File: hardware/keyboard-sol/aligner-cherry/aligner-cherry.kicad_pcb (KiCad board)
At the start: 2 copper layers, 386.1 x 117.7 mm, 94 parts, among them SW10 TAB: 1.25x, SW11 I, SW12 2, SW13 Zero, SW14 Q, SW15 O, SW16 3, SW17 Dash, SW18 W, SW19 P, SW20 4, SW21 Caret, SW22 E, SW23 AT, SW24 5, SW25 LT Bracket, SW26 R, SW27 Return: 1.5x, SW28 6, SW29 Backslash, SW30 T, SW31 Line Feed, SW32 7, SW33 RT Bracket, SW34 Y, SW35 Load, SW36 LT Ctrl, SW37 J, SW38 Upper Case: 1.5x, SW39 M, SW4 ESC: 1.75x, SW40 Shift Lock: 1.5x, SW41 K, SW42 LT Shift: 1.5x, SW43 Comma, SW44 A, SW45 L, SW46 Z, SW47 Period, SW48 S, SW49 Semicolon, SW5 8, SW50 X, SW51 Slash, SW52 D, SW53 Colon, SW54 C, SW55 RT Shift: 2x, SW56 F, SW57 DEL, SW58 V, SW59 Mode Select: 1.75x, SW6 BREAK, SW60 G, SW61 Repeat: 1.25x, SW62 B, SW63 H, SW64 RT Ctrl, SW65 N, SW66 Local, SW67 NP Dash, SW68 NP 4, SW69 NP Zero, SW7 U, SW70 Up Arrow, SW71 NP 7, SW72 NP 1, SW73 NP period, SW74 LT Arrow, SW75 NP asterisk, SW76 NP 5, SW77 NP plus, SW78 Spacebar, SW79 NP 8, SW8 1, SW80 NP 2, SW81 RT Arrow, SW82 NP divide, SW83 NP 6, SW84 Down Arrow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

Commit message: Moved mounting slots from keyboard PCB to aligners
- This allows the PCB to sink below the mounting brackets.  The aligner height can
be adjusted relative to the mounting brackets using spacers.

- changed futaba aligners to use cherry stabilizers.

- bumped rev number
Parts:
- SW55: footprint unikbd:Key_MX_Aligner -> unikbd:MX_2u_aligner
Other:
- board size 386.1 x 117.7 mm -> 428.6 x 117.7 mm
- board text added: "SOL-20 Cherry MX aligner Rev 1.1"
- board text removed: "SOL-20 Cherry MX aligner Rev 1.0"

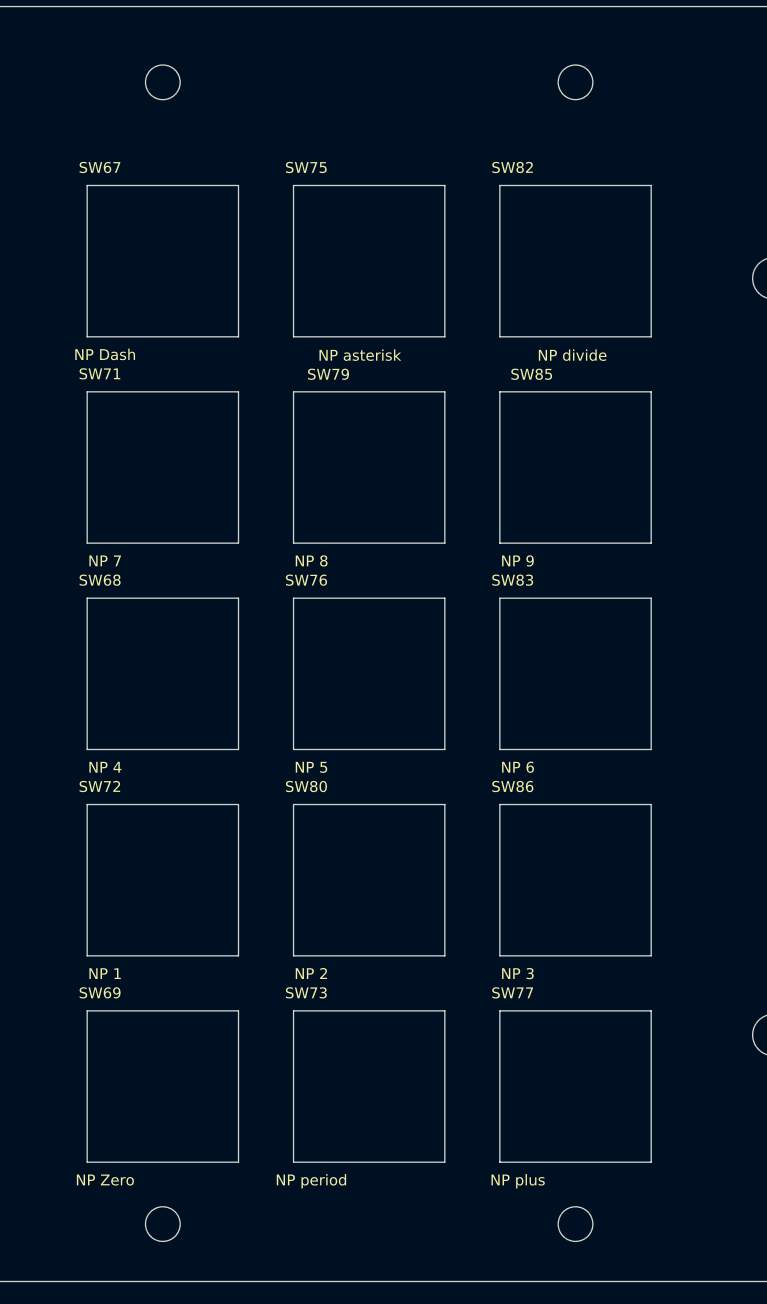
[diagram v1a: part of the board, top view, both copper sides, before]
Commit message: On aligners, moved numpad 0.1825" to the right.
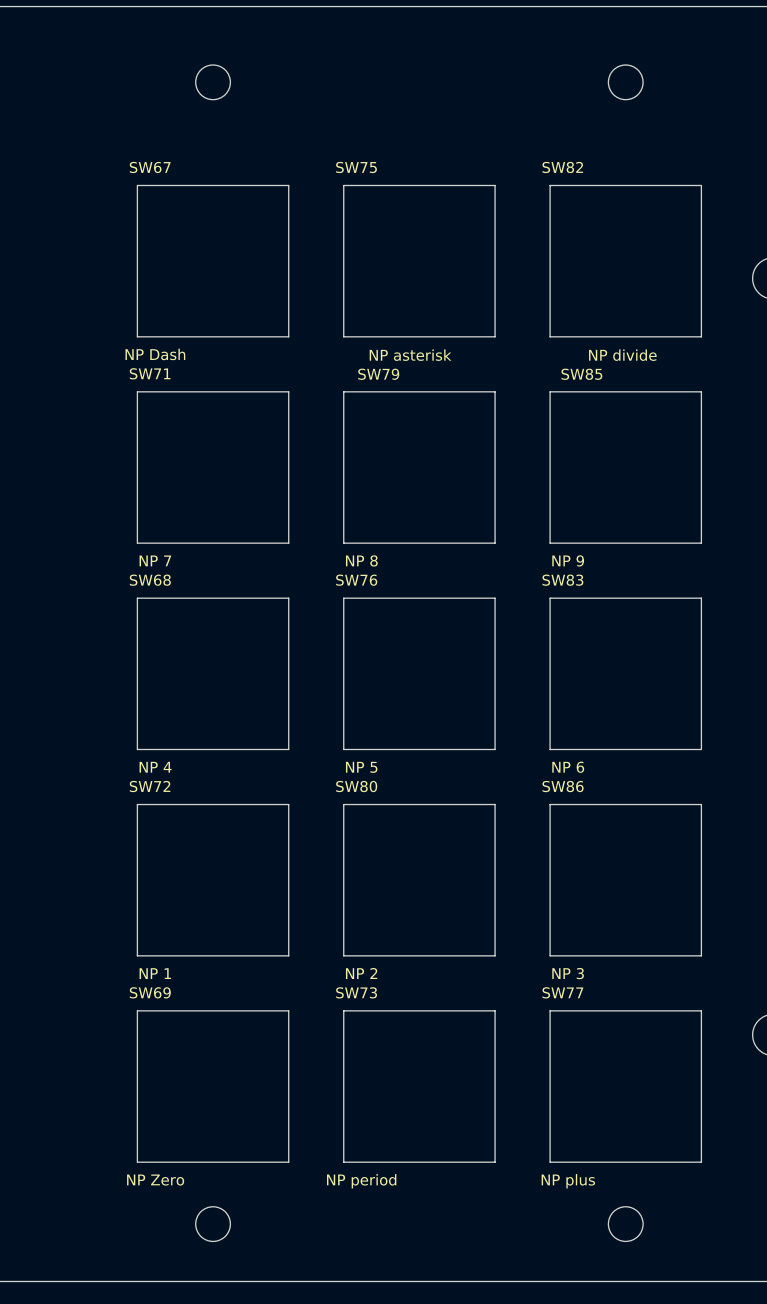
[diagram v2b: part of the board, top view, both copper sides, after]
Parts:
- removed the REF** at (432.4, 219.5)
- removed the REF** at (470.5, 219.5)
- removed the REF** at (470.5, 114.1)
- removed the REF** at (432.4, 114.1)
- added REF**: MountingHole_3.2mm_M3, MountingHole:MountingHole_3.2mm_M3, F.Cu at (437.1, 219.5)
- added REF**: MountingHole_3.2mm_M3, MountingHole:MountingHole_3.2mm_M3, F.Cu at (475.2, 219.5)
- added REF**: MountingHole_3.2mm_M3, MountingHole:MountingHole_3.2mm_M3, F.Cu at (475.2, 114.1)
- added REF**: MountingHole_3.2mm_M3, MountingHole:MountingHole_3.2mm_M3, F.Cu at (437.1, 114.1)
- moved SW73 4.64 mm to (456.1, 206.8)
- moved SW75 4.64 mm to (456.1, 130.6)
- moved SW76 4.64 mm to (456.1, 168.7)
- moved SW79 4.64 mm to (456.1, 149.6)
- moved SW80 4.64 mm to (456.1, 187.7)
- moved SW67 4.64 mm to (437.1, 130.6)
- moved SW68 4.64 mm to (437.1, 168.7)
- moved SW69 4.64 mm to (437.1, 206.8)
- moved SW71 4.64 mm to (437.1, 149.6)
- moved SW72 4.64 mm to (437.1, 187.7)
- moved SW77 4.64 mm to (475.2, 206.8)
- moved SW82 4.64 mm to (475.2, 130.6)
- moved SW83 4.64 mm to (475.2, 168.7)
- moved SW85 4.64 mm to (475.2, 149.6)
- moved SW86 4.64 mm to (475.2, 187.7)
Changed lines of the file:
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@@
   )
   (module unikbd:Key_MX_Aligner locked (layer F.Cu)
-    (at 451.47738 168.69156)
+    (at 456.11288 168.69156)
     (fp_text reference SW76 (at -5.7912 -8.6106) (layer F.SilkS)
       (effects (font (size 1 1) (thickness 0.15)))
@@
   )
   (module unikbd:Key_MX_Aligner locked (layer F.Cu)
-    (at 432.42738 168.69156)
+    (at 437.06288 168.69156)
     (fp_text reference SW68 (at -5.7912 -8.6106) (layer F.SilkS)
       (effects (font (size 1 1) (thickness 0.15)))
@@
   )
   (module unikbd:Key_MX_Aligner locked (layer F.Cu)
-    (at 470.52738 168.69156)
+    (at 475.16288 168.69156)
     (fp_text reference SW83 (at -5.7912 -8.6106) (layer F.SilkS)
       (effects (font (size 1 1) (thickness 0.15)))
@@
   )
   (module unikbd:Key_MX_Aligner locked (layer F.Cu)
-    (at 470.52738 149.64156)
+    (at 475.16288 149.64156)
     (fp_text reference SW85 (at -4.03098 -8.56996) (layer F.SilkS)
       (effects (font (size 1 1) (thickness 0.15)))
@@
   )
   (module unikbd:Key_MX_Aligner locked (layer F.Cu)
-    (at 470.52738 187.74156)
+    (at 475.16288 187.74156)
     (fp_text reference SW86 (at -5.7912 -8.6106) (layer F.SilkS)
       (effects (font (size 1 1) (thickness 0.15)))
@@
   )
   (module unikbd:Key_MX_Aligner locked (layer F.Cu)
-    (at 470.52738 130.59156)
+    (at 475.16288 130.59156)
     (fp_text reference SW82 (at -5.7912 -8.6106) (layer F.SilkS)
       (effects (font (size 1 1) (thickness 0.15)))
@@
   )
   (module unikbd:Key_MX_Aligner locked (layer F.Cu)
-    (at 451.47738 187.74156)
+    (at 456.11288 187.74156)
     (fp_text reference SW80 (at -5.7912 -8.6106) (layer F.SilkS)
       (effects (font (size 1 1) (thickness 0.15)))
@@
   )
   (module unikbd:Key_MX_Aligner locked (layer F.Cu)
-    (at 451.47738 149.64156)
+    (at 456.11288 149.64156)
     (fp_text reference SW79 (at -3.75158 -8.56996) (layer F.SilkS)
       (effects (font (size 1 1) (thickness 0.15)))
@@
   )
   (module unikbd:Key_MX_Aligner locked (layer F.Cu)
-    (at 470.52738 206.79156)
+    (at 475.16288 206.79156)
     (fp_text reference SW77 (at -5.7912 -8.6106) (layer F.SilkS)
       (effects (font (size 1 1) (thickness 0.15)))
@@
   )
   (module unikbd:Key_MX_Aligner locked (layer F.Cu)
-    (at 451.47738 130.59156)
+    (at 456.11288 130.59156)
     (fp_text reference SW75 (at -5.7912 -8.6106) (layer F.SilkS)
       (effects (font (size 1 1) (thickness 0.15)))
@@
   )
   (module unikbd:Key_MX_Aligner locked (layer F.Cu)
-    (at 451.47738 206.79156)
+    (at 456.11288 206.79156)
     (fp_text reference SW73 (at -5.7912 -8.6106) (layer F.SilkS)
       (effects (font (size 1 1) (thickness 0.15)))
@@
   )
   (module unikbd:Key_MX_Aligner locked (layer F.Cu)
-    (at 432.42738 187.74156)
+    (at 437.06288 187.74156)
     (fp_text reference SW72 (at -5.7912 -8.6106) (layer F.SilkS)
       (effects (font (size 1 1) (thickness 0.15)))
@@
   )
   (module unikbd:Key_MX_Aligner locked (layer F.Cu)
-    (at 432.42738 149.64156)
+    (at 437.06288 149.64156)
     (fp_text reference SW71 (at -5.7912 -8.6106) (layer F.SilkS)
       (effects (font (size 1 1) (thickness 0.15)))
@@
   )
   (module unikbd:Key_MX_Aligner locked (layer F.Cu)
-    (at 432.42738 206.79156)
+    (at 437.06288 206.79156)
     (fp_text reference SW69 (at -5.7912 -8.6106) (layer F.SilkS)
       (effects (font (size 1 1) (thickness 0.15)))
@@
   )
   (module unikbd:Key_MX_Aligner locked (layer F.Cu)
-    (at 432.42738 130.59156)
+    (at 437.06288 130.59156)
     (fp_text reference SW67 (at -5.7912 -8.6106) (layer F.SilkS)
       (effects (font (size 1 1) (thickness 0.15)))
@@
   )
   (module MountingHole:MountingHole_3.2mm_M3 locked (layer F.Cu)
-    (at 432.42738 219.49156)
+    (at 437.06288 219.49156)
     (descr "Mounting Hole 3.2mm, no annular, M3")
     (tags "mounting hole 3.2mm no annular m3")
@@
   )
   (module MountingHole:MountingHole_3.2mm_M3 locked (layer F.Cu)
-    (at 470.52738 219.49156)
+    (at 475.16288 219.49156)
     (descr "Mounting Hole 3.2mm, no annular, M3")
     (tags "mounting hole 3.2mm no annular m3")
@@
   )
   (module MountingHole:MountingHole_3.2mm_M3 locked (layer F.Cu)
-    (at 470.52738 114.08156)
+    (at 475.16288 114.08156)
     (descr "Mounting Hole 3.2mm, no annular, M3")
     (tags "mounting hole 3.2mm no annular m3")
@@
   )
   (module MountingHole:MountingHole_3.2mm_M3 locked (layer F.Cu)
-    (at 432.42738 114.08156)
+    (at 437.06288 114.08156)
     (descr "Mounting Hole 3.2mm, no annular, M3")
     (tags "mounting hole 3.2mm no annular m3")

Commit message: Adjsut mounting slots and alignment of mounting holes.
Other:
- outline, holes or cut-outs redrawn
- board text added: "SOL-20 Cherry MX aligner Rev 1.4"
- board text removed: "SOL-20 Cherry MX aligner Rev 1.1"
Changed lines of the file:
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@@
   (gr_circle (center 102.16388 187.74156) (end 105.38968 187.74156) (layer Edge.Cuts) (width 0.12))
   (gr_circle (center 121.21388 168.69156) (end 124.43968 168.69156) (layer Edge.Cuts) (width 0.12))
-  (gr_text "SOL-20 Cherry MX aligner  Rev 1.1\n" (at 140.9954 112.7506) (layer F.SilkS)
+  (gr_text "SOL-20 Cherry MX aligner  Rev 1.4\n" (at 140.9954 112.7506) (layer F.SilkS)
     (effects (font (size 2.032 2.032) (thickness 0.2032)) (justify left))
   )
@@
     (effects (font (size 2.032 2.032) (thickness 0.3048)) (justify left))
   )
-  (gr_line (start 505.45238 107.0864) (end 505.45238 130.27914) (layer Edge.Cuts) (width 0.1016))
-  (gr_line (start 505.45238 200.12914) (end 505.45238 134.08914) (layer Edge.Cuts) (width 0.1016))
-  (gr_line (start 505.45238 224.79) (end 505.45238 203.93914) (layer Edge.Cuts) (width 0.1016))
-  (gr_line (start 488.78109 203.93914) (end 505.44984 203.93914) (layer Edge.Cuts) (width 0.1016))
-  (gr_line (start 488.78109 134.08914) (end 505.44984 134.08914) (layer Edge.Cuts) (width 0.1016))
-  (gr_line (start 488.78109 130.27914) (end 505.44984 130.27914) (layer Edge.Cuts) (width 0.1016))
-  (gr_arc (start 488.78109 132.18414) (end 488.78109 130.27914) (angle -180) (layer Edge.Cuts) (width 0.1016))
-  (gr_line (start 488.78109 200.12914) (end 505.44984 200.12914) (layer Edge.Cuts) (width 0.1016))
-  (gr_arc (start 488.78109 202.03414) (end 488.78109 200.12914) (angle -180) (layer Edge.Cuts) (width 0.1016))
-  (gr_line (start 76.82738 134.08914) (end 76.82738 200.12914) (layer Edge.Cuts) (width 0.1016))
-  (gr_line (start 76.82738 107.0864) (end 76.82738 130.27914) (layer Edge.Cuts) (width 0.1016))
-  (gr_line (start 93.49613 130.27914) (end 76.82738 130.27914) (layer Edge.Cuts) (width 0.1016))
-  (gr_line (start 93.49613 134.08914) (end 76.82738 134.08914) (layer Edge.Cuts) (width 0.1016))
-  (gr_arc (start 93.49613 132.18414) (end 93.49613 130.27914) (angle 180) (layer Edge.Cuts) (width 0.1016))
-  (gr_line (start 93.49613 203.93914) (end 76.82738 203.93914) (layer Edge.Cuts) (width 0.1016))
-  (gr_line (start 93.49613 200.12914) (end 76.82738 200.12914) (layer Edge.Cuts) (width 0.1016))
-  (gr_line (start 76.82738 224.79) (end 76.82738 203.93914) (layer Edge.Cuts) (width 0.1016))
-  (gr_arc (start 93.49613 202.03414) (end 93.49613 200.12914) (angle 180) (layer Edge.Cuts) (width 0.1016))
+  (gr_line (start 505.45238 107.0864) (end 505.45238 132.81914) (layer Edge.Cuts) (width 0.1016))
+  (gr_line (start 505.45238 202.66914) (end 505.45238 136.62914) (layer Edge.Cuts) (width 0.1016))
+  (gr_line (start 505.45238 224.79) (end 505.45238 206.47914) (layer Edge.Cuts) (width 0.1016))
+  (gr_line (start 488.78109 206.47914) (end 505.44984 206.47914) (layer Edge.Cuts) (width 0.1016))
+  (gr_line (start 488.78109 136.62914) (end 505.44984 136.62914) (layer Edge.Cuts) (width 0.1016))
+  (gr_line (start 488.78109 132.81914) (end 505.44984 132.81914) (layer Edge.Cuts) (width 0.1016))
+  (gr_arc (start 488.78109 134.72414) (end 488.78109 132.81914) (angle -180) (layer Edge.Cuts) (width 0.1016))
+  (gr_line (start 488.78109 202.66914) (end 505.44984 202.66914) (layer Edge.Cuts) (width 0.1016))
+  (gr_arc (start 488.78109 204.57414) (end 488.78109 202.66914) (angle -180) (layer Edge.Cuts) (width 0.1016))
+  (gr_line (start 76.82738 136.62914) (end 76.82738 202.66914) (layer Edge.Cuts) (width 0.1016))
+  (gr_line (start 76.82738 107.0864) (end 76.82738 132.81914) (layer Edge.Cuts) (width 0.1016))
+  (gr_line (start 93.49613 132.81914) (end 76.82738 132.81914) (layer Edge.Cuts) (width 0.1016))
+  (gr_line (start 93.49613 136.62914) (end 76.82738 136.62914) (layer Edge.Cuts) (width 0.1016))
+  (gr_arc (start 93.49613 134.72414) (end 93.49613 132.81914) (angle 180) (layer Edge.Cuts) (width 0.1016))
+  (gr_line (start 93.49613 206.47914) (end 76.82738 206.47914) (layer Edge.Cuts) (width 0.1016))
+  (gr_line (start 93.49613 202.66914) (end 76.82738 202.66914) (layer Edge.Cuts) (width 0.1016))
+  (gr_line (start 76.82738 224.79) (end 76.82738 206.47914) (layer Edge.Cuts) (width 0.1016))
+  (gr_arc (start 93.49613 204.57414) (end 93.49613 202.66914) (angle 180) (layer Edge.Cuts) (width 0.1016))
   (gr_line (start 76.82738 224.79) (end 505.45238 224.79) (layer Edge.Cuts) (width 0.1))
   (gr_line (start 505.45238 107.0864) (end 76.82738 107.0864) (layer Edge.Cuts) (width 0.1016))

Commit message: Added stabilizer bending guide and futaba stabilizer posts to PCB
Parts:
- added REF**: Stabilizer sizing hole, MountingHole:MountingHole_2.1mm, F.Cu at (318.2, 219.2)
- added REF**: Stabilizer sizing hole, MountingHole:MountingHole_2.1mm, F.Cu at (184.8, 219.2)
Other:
- board text added: "Stabilizer bar sizing guide"
- board text added: "Unified Keyboard Project."
- board text added: "https://github.com/osiweb/unified_retro_keyboard"
- board text removed: "Unified Keyboard Project. https://github.com/osiweb/unified_retro_keyboard"

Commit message: Update Sol-20 keyboard to use fixed footprints
- Update all footprints on sol-20 keyboard and aligners

- Add soldermask clearance around cherry MX posts

- Move Cherry MX pads down 1 mil, and Futaba pads up 2 mils

- Adjust Cherry aligner footprints down 1 mil

- Adjust Futaba aligner footprints up 2 mils

- Move mounting slots up 1 mil on Cherry aligner

- Move mounting slots down 1 mil on Futaba aligner

- incorporate improved stabilizer post adapters in futaba aligner

- add slots for stabilizer posts in futaba aligner and Sol kebyoard PCB

- Move stabilizer bar bend guide to left bottom edge to facilitate bending

- Bump rev to 1.6
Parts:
- removed the REF** at (184.8, 219.2)
- moved REF** 108.0 mm to (210.2, 220.6)
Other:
- outline, holes or cut-outs redrawn
- board text added: "SOL-20 Cherry MX aligner Rev 1.6"
- board text removed: "SOL-20 Cherry MX aligner Rev 1.4"

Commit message: Moved Cherry MX and futaba pads farther apart in combined footprint
- Offset cherry MX pads and aligners downward 0.004" from origin

- Offset futaba pads and aligners upward -0.004" from origin

- Update footprints in classic and sol-20 pcbs and aligners

- adjust mounting slots in Sol-20 aligners to match futaba or cherry offset
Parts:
- moved REF** 0.08 mm to (210.2, 220.7)
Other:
- outline, holes or cut-outs redrawn
- board text added: "SOL-20 Cherry MX aligner Rev 1.7"
- board text removed: "SOL-20 Cherry MX aligner Rev 1.6"
